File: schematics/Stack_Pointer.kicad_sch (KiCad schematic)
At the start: 43 parts, among them U1 74LS283, U10 74LS30, U11 74LS32, U12 74LS00, U13 74LS00, U14 74LS08, U2 74LS173, U3 74LS283, U4 74LS173, U5 74LS32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

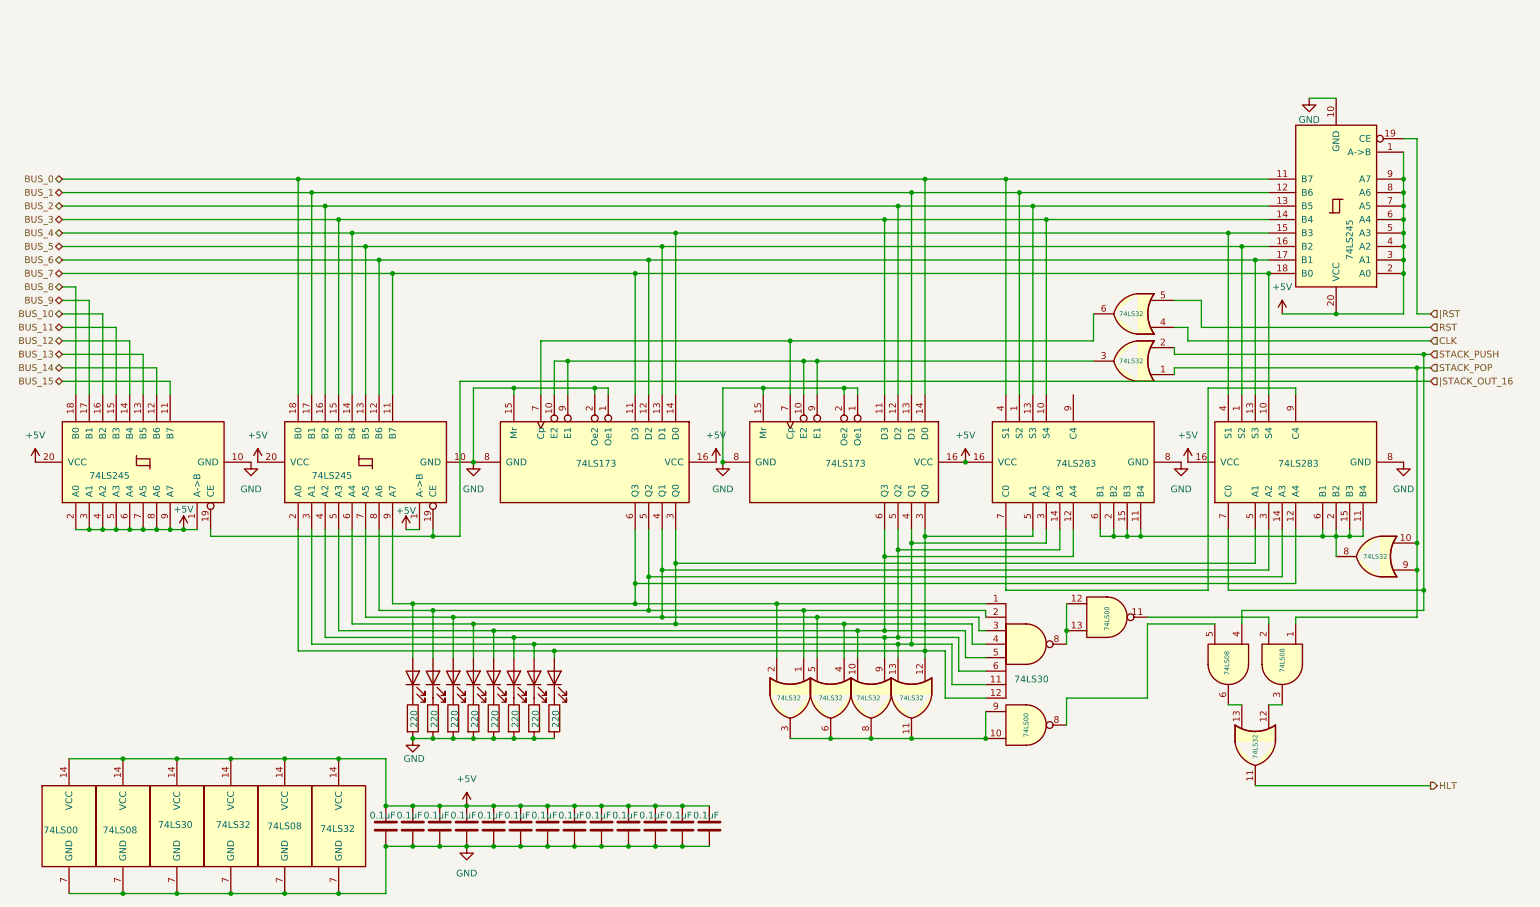
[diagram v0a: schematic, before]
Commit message: feat: updated stack pointer to use 1 IC instead of 2 for each counter
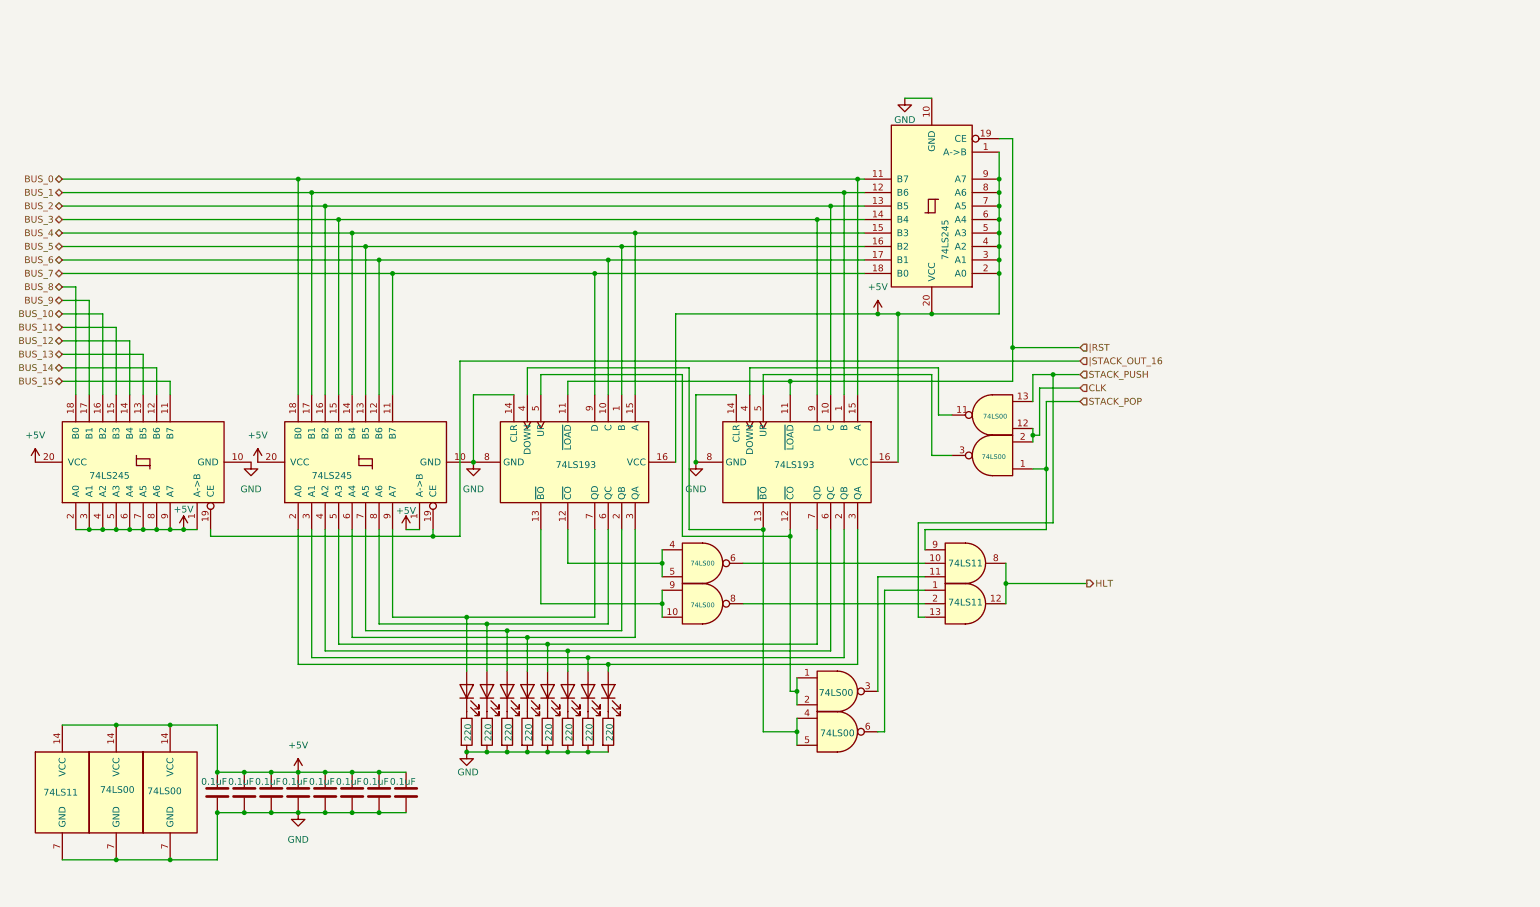
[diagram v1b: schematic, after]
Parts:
- removed C10, C11, C12, C13, C9: 0.1uF, symbol Device:C
- removed U1, U3: 74LS283, symbol 74xx:74LS283
- removed U10: 74LS30, symbol 74xx:74LS30
- removed U11, U5: 74LS32, symbol 74xx:74LS32
- removed U12, U13: 74LS00, symbol 74xx:74LS00
- removed U14, U9: 74LS08, symbol 74xx:74LS08
- removed U2, U4: 74LS173, symbol 74xx:74LS173
- added U15, U16: 74LS193, symbol 74xx:74LS193
- added U2, U3: 74LS00, symbol 74xx:74LS00
- added U4: 74LS11, symbol 74xx:74LS11
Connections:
- net +5V: now also U15.16 (VCC), U16.16 (VCC), U2.14 (VCC), U3.14 (VCC), U4.14 (VCC)
- net BUS_0: now also U15.15 (A)
- net BUS_1: now also U15.1 (B)
- net BUS_2: now also U15.10 (C)
- net BUS_3: now also U15.9 (D)
- net BUS_4: now also U16.15 (A)
- net BUS_5: now also U16.1 (B)
- net BUS_6: now also U16.10 (C)
- net BUS_7: now also U16.9 (D)
- net CLK: now also U2.12, U2.2
- net GND: now also U15.14 (CLR), U15.8 (GND), U16.14 (CLR), U16.8 (GND), U2.7 (GND), U3.7 (GND), U4.7 (GND)
- net HLT: now also U4.12, U4.8
- net STACK_POP: now also U2.1, U4.9
- net STACK_PUSH: now also U2.13, U4.13
- net |RST: now also U15.11 (~{LOAD}), U16.11 (~{LOAD})
- net at D16.2 (A), U6.2 (A0): now also U15.3 (QA)
- net at D10.2 (A), U6.8 (A6): now also U16.6 (QC)
- net at D9.2 (A), U6.9 (A7): now also U16.7 (QD)
- net at D13.2 (A), U6.5 (A3): now also U15.7 (QD)
- net at D14.2 (A), U6.4 (A2): now also U15.6 (QC)
- net at D15.2 (A), U6.3 (A1): now also U15.2 (QB)
- net at D12.2 (A), U6.6 (A4): now also U16.3 (QA)
- net at D11.2 (A), U6.7 (A5): now also U16.2 (QB)
- new net: U16.12 (~{CO}), U2.4, U2.5
- new net: U16.13 (~{BO}), U2.10, U2.9
- new net: U15.13 (~{BO}), U16.4 (DOWN), U3.4, U3.5
- new net: U15.12 (~{CO}), U16.5 (UP), U3.1, U3.2
- new net: U3.6, U4.1
- new net: U15.4 (DOWN), U2.11
- new net: U2.6, U4.10
- new net: U15.5 (UP), U2.3
- new net: U3.3, U4.11
- new net: U2.8, U4.2

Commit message: Updated schematics and README
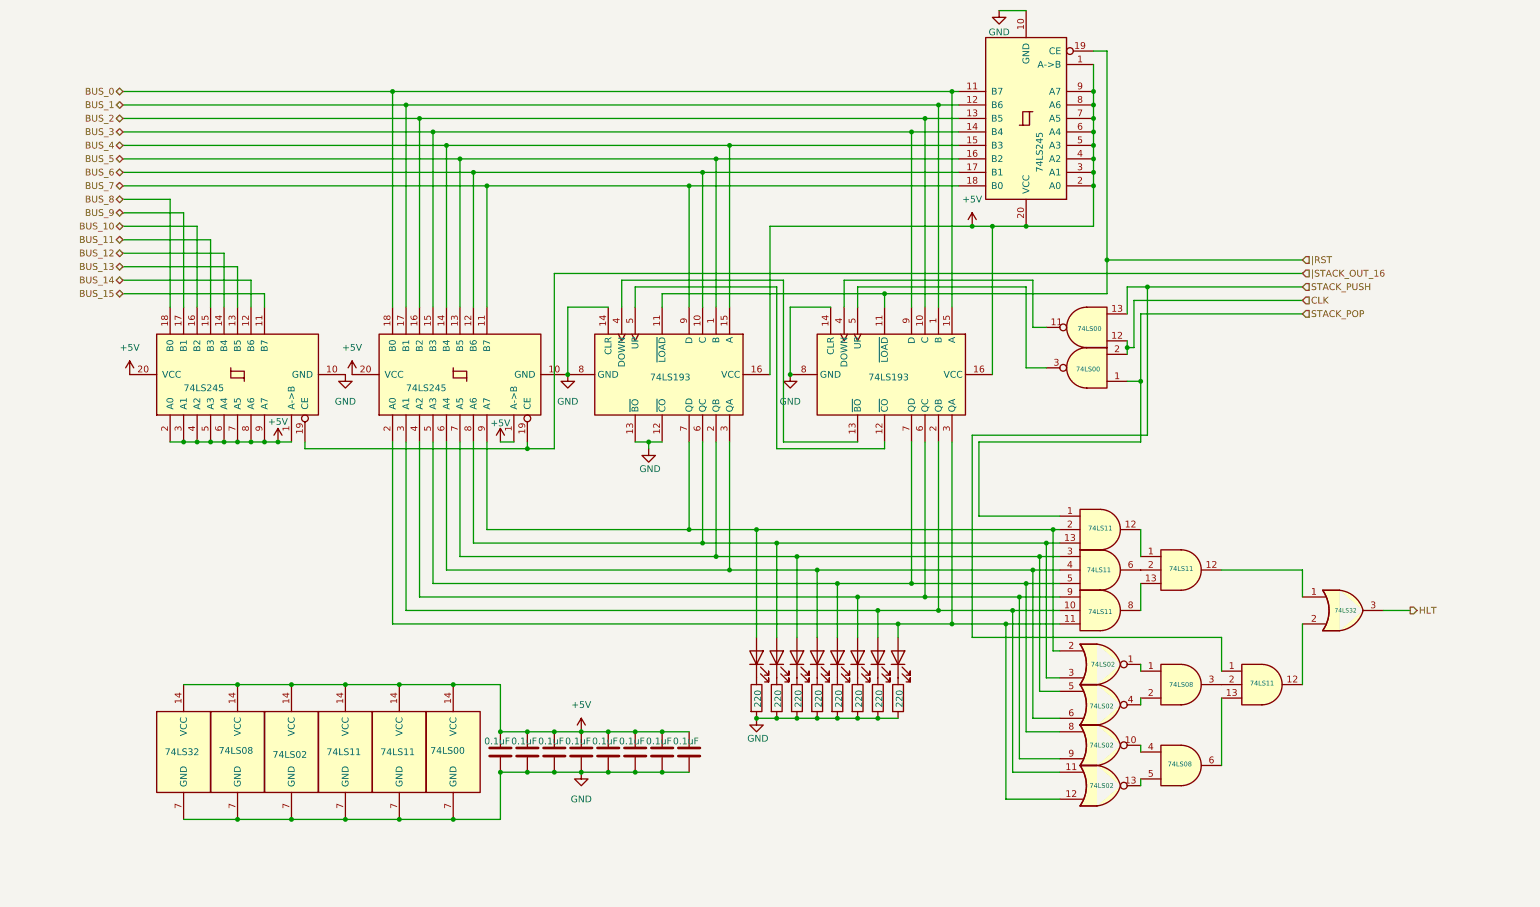
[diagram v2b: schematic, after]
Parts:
- removed unit 2 of U2
- removed unit 5 of U2
- removed unit 3 of U2
- removed unit 2 of U3
- removed unit 1 of U3
- removed unit 3 of U4
- added U1, U9: 74LS11, symbol 74xx:74LS11
- added U10: 74LS08, symbol 74xx:74LS08
- added U11: 74LS32, symbol 74xx:74LS32
- added U5: 74LS02, symbol 74xx:74LS02
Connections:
- net +5V: now also U1.14 (VCC), U10.14 (VCC), U11.14 (VCC), U5.14 (VCC)
- net GND: now also U16.12 (~{CO}), U16.13 (~{BO}), U1.7 (GND), U10.7 (GND), U11.7 (GND), U5.7 (GND)
- net HLT: now also U11.3; no longer U4.12
- net STACK_POP: now also U1.1
- net STACK_PUSH: now also U9.1; no longer U4.13
- net at D16.2 (A), U15.3 (QA), U6.2 (A0): now also U1.11, U5.12
- net at D12.2 (A), U16.3 (QA), U6.6 (A4): now also U1.4, U5.6
- net at D13.2 (A), U15.7 (QD), U6.5 (A3): now also U1.5, U5.8
- net at D11.2 (A), U16.2 (QB), U6.7 (A5): now also U1.3, U5.5
- net at D10.2 (A), U16.6 (QC), U6.8 (A6): now also U1.13, U5.3
- net at D9.2 (A), U16.7 (QD), U6.9 (A7): now also U1.2, U5.2
- net at U4.1: now also U1.12
- net at D15.2 (A), U15.2 (QB), U6.3 (A1): now also U1.10, U5.11
- net at D14.2 (A), U15.6 (QC), U6.4 (A2): now also U1.9, U5.9
- net at U4.2: now also U1.6
- new net: U10.1, U5.1
- new net: U10.2, U5.4
- new net: U10.3, U9.2
- new net: U10.5, U5.13
- new net: U11.2, U9.12
- new net: U10.6, U9.13
- new net: U11.1, U4.12
- new net: U1.8, U4.13
- new net: U10.4, U5.10
